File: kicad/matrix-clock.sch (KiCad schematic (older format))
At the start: 158 parts, among them P1 CONN_02X08, P2 CONN_01X03

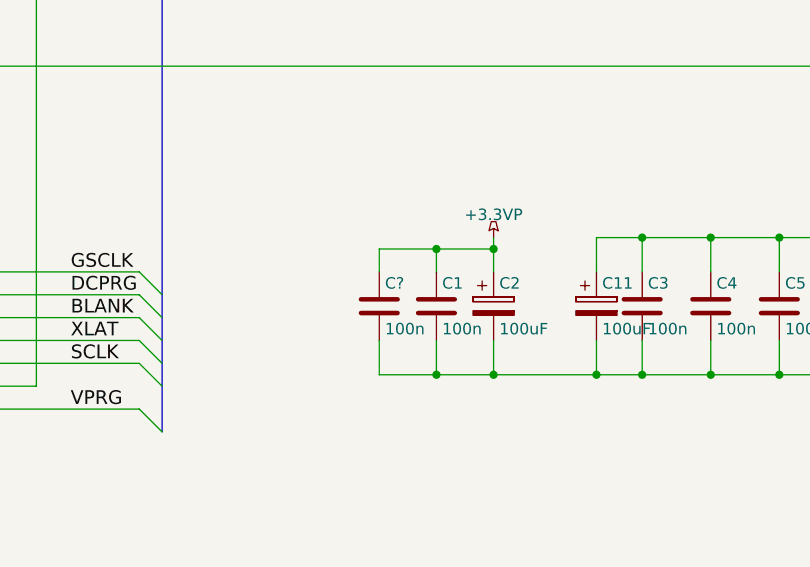
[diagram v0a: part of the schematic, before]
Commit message: removed libs
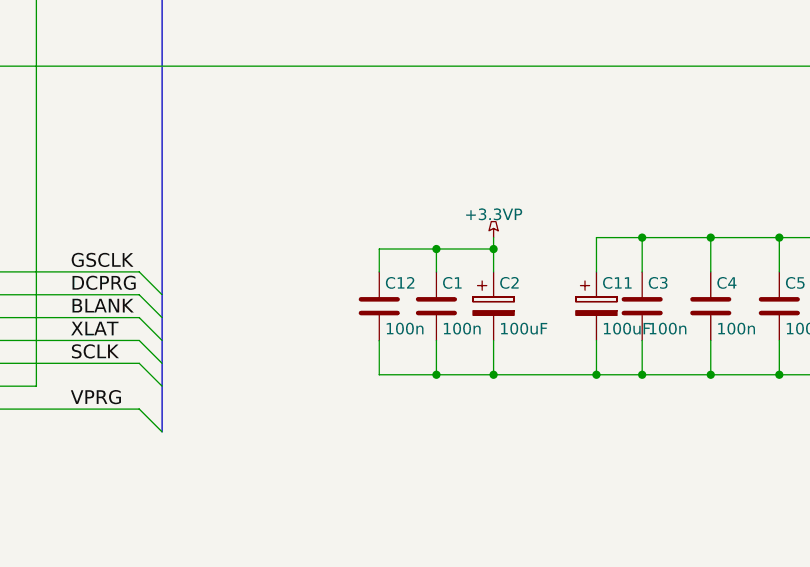
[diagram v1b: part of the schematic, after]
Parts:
- gave numbers to parts that had none: 1
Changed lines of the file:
@@
 LIBS:contrib
 LIBS:valves
-LIBS:IHE
-LIBS:open-project
 LIBS:matrix-clock-cache
 EELAYER 25 0
@@
 $EndComp
 $Comp
-L GND #PWR01
+L GND #PWR3
 U 1 1 57FAE61F
 P 1250 3050
-F 0 "#PWR01" H 1250 2800 50  0001 C CNN
+F 0 "#PWR3" H 1250 2800 50  0001 C CNN
 F 1 "GND" H 1250 2900 50  0000 C CNN
 F 2 "" H 1250 3050 50  0000 C CNN
@@
 $EndComp
 $Comp
-L +3.3VP #PWR02
+L +3.3VP #PWR1
 U 1 1 57FAE666
 P 650 650
-F 0 "#PWR02" H 800 600 50  0001 C CNN
+F 0 "#PWR1" H 800 600 50  0001 C CNN
 F 1 "+3.3VP" H 650 750 50  0000 C CNN
 F 2 "" H 650 650 50  0000 C CNN
@@
 $EndComp
 $Comp
-L +3.3V #PWR03
+L +3.3V #PWR5
 U 1 1 57FAE778
 P 1350 3250
-F 0 "#PWR03" H 1350 3100 50  0001 C CNN
+F 0 "#PWR5" H 1350 3100 50  0001 C CNN
 F 1 "+3.3V" H 1350 3390 50  0000 C CNN
 F 2 "" H 1350 3250 50  0000 C CNN
@@
 $EndComp
 $Comp
-L GND #PWR04
+L GND #PWR7
 U 1 1 57FAEBAA
 P 1550 3350
-F 0 "#PWR04" H 1550 3100 50  0001 C CNN
+F 0 "#PWR7" H 1550 3100 50  0001 C CNN
 F 1 "GND" H 1550 3200 50  0000 C CNN
 F 2 "" H 1550 3350 50  0000 C CNN
@@
 $EndComp
 $Comp
-L GND #PWR05
+L GND #PWR10
 U 1 1 57FB4A6F
 P 3000 3050
-F 0 "#PWR05" H 3000 2800 50  0001 C CNN
+F 0 "#PWR10" H 3000 2800 50  0001 C CNN
 F 1 "GND" H 3000 2900 50  0000 C CNN
 F 2 "" H 3000 3050 50  0000 C CNN
@@
 $EndComp
 $Comp
-L +3.3V #PWR06
+L +3.3V #PWR12
 U 1 1 57FB4A7B
 P 3100 3250
-F 0 "#PWR06" H 3100 3100 50  0001 C CNN
+F 0 "#PWR12" H 3100 3100 50  0001 C CNN
 F 1 "+3.3V" H 3100 3390 50  0000 C CNN
 F 2 "" H 3100 3250 50  0000 C CNN
@@
 $EndComp
 $Comp
-L GND #PWR07
+L GND #PWR14
 U 1 1 57FB4A89
 P 3300 3350
-F 0 "#PWR07" H 3300 3100 50  0001 C CNN
+F 0 "#PWR14" H 3300 3100 50  0001 C CNN
 F 1 "GND" H 3300 3200 50  0000 C CNN
 F 2 "" H 3300 3350 50  0000 C CNN
@@
 $EndComp
 $Comp
-L GND #PWR08
+L GND #PWR17
 U 1 1 57FB6FB4
 P 4750 3050
-F 0 "#PWR08" H 4750 2800 50  0001 C CNN
+F 0 "#PWR17" H 4750 2800 50  0001 C CNN
 F 1 "GND" H 4750 2900 50  0000 C CNN
 F 2 "" H 4750 3050 50  0000 C CNN
@@
 $EndComp
 $Comp
-L +3.3V #PWR09
+L +3.3V #PWR19
 U 1 1 57FB6FC0
 P 4850 3250
-F 0 "#PWR09" H 4850 3100 50  0001 C CNN
+F 0 "#PWR19" H 4850 3100 50  0001 C CNN
 F 1 "+3.3V" H 4850 3390 50  0000 C CNN
 F 2 "" H 4850 3250 50  0000 C CNN
@@
 $EndComp
 $Comp
-L GND #PWR010
+L GND #PWR20
 U 1 1 57FB6FCE
 P 5050 3350
-F 0 "#PWR010" H 5050 3100 50  0001 C CNN
+F 0 "#PWR20" H 5050 3100 50  0001 C CNN
 F 1 "GND" H 5050 3200 50  0000 C CNN
 F 2 "" H 5050 3350 50  0000 C CNN
@@
 $EndComp
 $Comp
-L GND #PWR011
+L GND #PWR22
 U 1 1 57FB707E
 P 6500 3050
-F 0 "#PWR011" H 6500 2800 50  0001 C CNN
+F 0 "#PWR22" H 6500 2800 50  0001 C CNN
 F 1 "GND" H 6500 2900 50  0000 C CNN
 F 2 "" H 6500 3050 50  0000 C CNN
@@
 $EndComp
 $Comp
-L +3.3V #PWR012
+L +3.3V #PWR23
 U 1 1 57FB7084
 P 6600 3250
-F 0 "#PWR012" H 6600 3100 50  0001 C CNN
+F 0 "#PWR23" H 6600 3100 50  0001 C CNN
 F 1 "+3.3V" H 6600 3390 50  0000 C CNN
 F 2 "" H 6600 3250 50  0000 C CNN
@@
 $EndComp
 $Comp
-L GND #PWR013
+L GND #PWR24
 U 1 1 57FB7092
 P 6800 3350
-F 0 "#PWR013" H 6800 3100 50  0001 C CNN
+F 0 "#PWR24" H 6800 3100 50  0001 C CNN
 F 1 "GND" H 6800 3200 50  0000 C CNN
 F 2 "" H 6800 3350 50  0000 C CNN
@@
 VPRG
 $Comp
-L GND #PWR014
+L GND #PWR35
 U 1 1 57FBA91D
 P 10600 6000
-F 0 "#PWR014" H 10600 5750 50  0001 C CNN
+F 0 "#PWR35" H 10600 5750 50  0001 C CNN
 F 1 "GND" H 10600 5850 50  0000 C CNN
 F 2 "" H 10600 6000 50  0000 C CNN
@@
 $EndComp
 $Comp
-L +3.3V #PWR015
+L +3.3V #PWR34
 U 1 1 57FBAA15
 P 10600 5400
-F 0 "#PWR015" H 10600 5250 50  0001 C CNN
+F 0 "#PWR34" H 10600 5250 50  0001 C CNN
 F 1 "+3.3V" H 10600 5540 50  0000 C CNN
 F 2 "" H 10600 5400 50  0000 C CNN
@@
 $EndComp
 $Comp
-L GND #PWR016
+L GND #PWR27
 U 1 1 57FC3799
 P 8250 3050
-F 0 "#PWR016" H 8250 2800 50  0001 C CNN
+F 0 "#PWR27" H 8250 2800 50  0001 C CNN
 F 1 "GND" H 8250 2900 50  0000 C CNN
 F 2 "" H 8250 3050 50  0000 C CNN
@@
 $EndComp
 $Comp
-L +3.3V #PWR017
+L +3.3V #PWR28
 U 1 1 57FC379F
 P 8350 3250
-F 0 "#PWR017" H 8350 3100 50  0001 C CNN
+F 0 "#PWR28" H 8350 3100 50  0001 C CNN
 F 1 "+3.3V" H 8350 3390 50  0000 C CNN
 F 2 "" H 8350 3250 50  0000 C CNN
@@
 $EndComp
 $Comp
-L GND #PWR018
+L GND #PWR29
 U 1 1 57FC37AB
 P 8550 3350
-F 0 "#PWR018" H 8550 3100 50  0001 C CNN
+F 0 "#PWR29" H 8550 3100 50  0001 C CNN
 F 1 "GND" H 8550 3200 50  0000 C CNN
 F 2 "" H 8550 3350 50  0000 C CNN
@@
 $EndComp
 $Comp
-L GND #PWR019
+L GND #PWR31
 U 1 1 57FC44F1
 P 10000 3050
-F 0 "#PWR019" H 10000 2800 50  0001 C CNN
+F 0 "#PWR31" H 10000 2800 50  0001 C CNN
 F 1 "GND" H 10000 2900 50  0000 C CNN
 F 2 "" H 10000 3050 50  0000 C CNN
@@
 $EndComp
 $Comp
-L +3.3V #PWR020
+L +3.3V #PWR32
 U 1 1 57FC44F7
 P 10100 3250
-F 0 "#PWR020" H 10100 3100 50  0001 C CNN
+F 0 "#PWR32" H 10100 3100 50  0001 C CNN
 F 1 "+3.3V" H 10100 3390 50  0000 C CNN
 F 2 "" H 10100 3250 50  0000 C CNN
@@
 $EndComp
 $Comp
-L GND #PWR021
+L GND #PWR33
 U 1 1 57FC4503
 P 10300 3350
-F 0 "#PWR021" H 10300 3100 50  0001 C CNN
+F 0 "#PWR33" H 10300 3100 50  0001 C CNN
 F 1 "GND" H 10300 3200 50  0000 C CNN
 F 2 "" H 10300 3350 50  0000 C CNN
@@
 DCPRG
 $Comp
-L +3.3VP #PWR022
+L +3.3VP #PWR25
 U 1 1 57FD372C
 P 7600 5400
-F 0 "#PWR022" H 7750 5350 50  0001 C CNN
+F 0 "#PWR25" H 7750 5350 50  0001 C CNN
 F 1 "+3.3VP" H 7600 5500 50  0000 C CNN
 F 2 "" H 7600 5400 50  0000 C CNN
@@
 $EndComp
 $Comp
-L GND #PWR023
+L GND #PWR4
 U 1 1 57FDA5D3
 P 1250 5150
-F 0 "#PWR023" H 1250 4900 50  0001 C CNN
+F 0 "#PWR4" H 1250 4900 50  0001 C CNN
 F 1 "GND" H 1250 5000 50  0000 C CNN
 F 2 "" H 1250 5150 50  0000 C CNN
@@
 $EndComp
 $Comp
-L +3.3V #PWR024
+L +3.3V #PWR6
 U 1 1 57FDA5DF
 P 1350 4950
-F 0 "#PWR024" H 1350 4800 50  0001 C CNN
+F 0 "#PWR6" H 1350 4800 50  0001 C CNN
 F 1 "+3.3V" H 1350 5090 50  0000 C CNN
 F 2 "" H 1350 4950 50  0000 C CNN
@@
 $EndComp
 $Comp
-L GND #PWR025
+L GND #PWR8
 U 1 1 57FDA5EB
 P 1550 4900
-F 0 "#PWR025" H 1550 4650 50  0001 C CNN
+F 0 "#PWR8" H 1550 4650 50  0001 C CNN
 F 1 "GND" H 1550 4750 50  0000 C CNN
 F 2 "" H 1550 4900 50  0000 C CNN
@@
 $EndComp
 $Comp
-L GND #PWR026
+L GND #PWR11
 U 1 1 57FDA663
 P 3000 5150
-F 0 "#PWR026" H 3000 4900 50  0001 C CNN
+F 0 "#PWR11" H 3000 4900 50  0001 C CNN
 F 1 "GND" H 3000 5000 50  0000 C CNN
 F 2 "" H 3000 5150 50  0000 C CNN
@@
 $EndComp
 $Comp
-L +3.3V #PWR027
+L +3.3V #PWR13
 U 1 1 57FDA669
 P 3100 4950
-F 0 "#PWR027" H 3100 4800 50  0001 C CNN
+F 0 "#PWR13" H 3100 4800 50  0001 C CNN
 F 1 "+3.3V" H 3100 5090 50  0000 C CNN
 F 2 "" H 3100 4950 50  0000 C CNN
@@
 $EndComp
 $Comp
-L GND #PWR028
+L GND #PWR15
 U 1 1 57FDA675
 P 3300 4900
-F 0 "#PWR028" H 3300 4650 50  0001 C CNN
+F 0 "#PWR15" H 3300 4650 50  0001 C CNN
 F 1 "GND" H 3300 4750 50  0000 C CNN
 F 2 "" H 3300 4900 50  0000 C CNN
@@
 $EndComp
 $Comp
-L +3.3VP #PWR029
+L +3.3VP #PWR2
 U 1 1 57FF26B5
 P 650 7400
-F 0 "#PWR029" H 800 7350 50  0001 C CNN
+F 0 "#PWR2" H 800 7350 50  0001 C CNN
 F 1 "+3.3VP" H 650 7500 50  0000 C CNN
 F 2 "" H 650 7400 50  0000 C CNN
@@
 $EndComp
 $Comp
-L +3.3VP #PWR030
+L +3.3VP #PWR9
 U 1 1 57FF3E3B
 P 2400 650
-F 0 "#PWR030" H 2550 600 50  0001 C CNN
+F 0 "#PWR9" H 2550 600 50  0001 C CNN
 F 1 "+3.3VP" H 2400 750 50  0000 C CNN
 F 2 "" H 2400 650 50  0000 C CNN
@@
 $EndComp
 $Comp
-L +3.3VP #PWR031
+L +3.3VP #PWR16
 U 1 1 57FF4355
 P 4150 650
-F 0 "#PWR031" H 4300 600 50  0001 C CNN
+F 0 "#PWR16" H 4300 600 50  0001 C CNN
 F 1 "+3.3VP" H 4150 750 50  0000 C CNN
 F 2 "" H 4150 650 50  0000 C CNN
@@
 $EndComp
 $Comp
-L +3.3VP #PWR032
+L +3.3VP #PWR21
 U 1 1 57FF4834
 P 5900 650
-F 0 "#PWR032" H 6050 600 50  0001 C CNN
+F 0 "#PWR21" H 6050 600 50  0001 C CNN
 F 1 "+3.3VP" H 5900 750 50  0000 C CNN
 F 2 "" H 5900 650 50  0000 C CNN
@@
 $EndComp
 $Comp
-L +3.3VP #PWR033
+L +3.3VP #PWR26
 U 1 1 57FF557A
 P 7650 650
-F 0 "#PWR033" H 7800 600 50  0001 C CNN
+F 0 "#PWR26" H 7800 600 50  0001 C CNN
 F 1 "+3.3VP" H 7650 750 50  0000 C CNN
 F 2 "" H 7650 650 50  0000 C CNN
@@
 $EndComp
 $Comp
-L +3.3VP #PWR034
+L +3.3VP #PWR30
 U 1 1 57FF5BD9
 P 9400 650
-F 0 "#PWR034" H 9550 600 50  0001 C CNN
+F 0 "#PWR30" H 9550 600 50  0001 C CNN
 F 1 "+3.3VP" H 9400 750 50  0000 C CNN
 F 2 "" H 9400 650 50  0000 C CNN
@@
 $EndComp
 $Comp
-L GND #PWR035
+L GND #PWR18
 U 1 1 5800335E
 P 4800 6350
-F 0 "#PWR035" H 4800 6100 50  0001 C CNN
+F 0 "#PWR18" H 4800 6100 50  0001 C CNN
 F 1 "GND" H 4800 6200 50  0000 C CNN
 F 2 "" H 4800 6350 50  0000 C CNN
@@
 $EndComp
 $Comp
-L +3.3VP #PWR036
+L +3.3VP #PWR36
 U 1 1 58017B29
 P 10650 5800
-F 0 "#PWR036" H 10800 5750 50  0001 C CNN
+F 0 "#PWR36" H 10800 5750 50  0001 C CNN
 F 1 "+3.3VP" H 10650 5900 50  0000 C CNN
 F 2 "" H 10650 5800 50  0000 C CNN
@@
 $EndComp
 $Comp
-L C C?
+L C C12
 U 1 1 5801A712
 P 7100 5700
-F 0 "C?" H 7125 5800 50  0000 L CNN
+F 0 "C12" H 7125 5800 50  0000 L CNN
 F 1 "100n" H 7125 5600 50  0000 L CNN
 F 2 "Capacitors_SMD:C_0603_HandSoldering" H 7138 5550 50  0001 C CNN

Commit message: pcb fixes
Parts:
- removed C12: 100n, Capacitors_SMD:C_0603_HandSoldering, symbol C
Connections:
- net BLANK: now also P1.10 (P10); no longer P1.8 (P8)
- net DCPRG: now also P1.12 (P12); no longer P1.6 (P6)
- net GND: no longer C1.2, C10.2, C11.2, C2.2, C3.2, C4.2, C5.2, C6.2, C7.2, C8.2, C9.2
- net GSCLK: now also P1.14 (P14); no longer P1.4 (P4)
- net SCLK: now also P1.6 (P6); no longer P1.12 (P12)
- net VPRG: now also P1.2 (P2); no longer P1.16 (P16)
- net XLAT: now also P1.8 (P8); no longer P1.10 (P10)
- net at TLC1.26 (SIN): now also P1.4 (P4); no longer P1.14 (P14)
- new net: C1.2, C2.2
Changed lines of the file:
@@
 $EndComp
 $Comp
-L GND #PWR3
+L GND #PWR01
 U 1 1 57FAE61F
 P 1250 3050
-F 0 "#PWR3" H 1250 2800 50  0001 C CNN
+F 0 "#PWR01" H 1250 2800 50  0001 C CNN
 F 1 "GND" H 1250 2900 50  0000 C CNN
 F 2 "" H 1250 3050 50  0000 C CNN
@@
 $EndComp
 $Comp
-L +3.3VP #PWR1
+L +3.3VP #PWR02
 U 1 1 57FAE666
 P 650 650
-F 0 "#PWR1" H 800 600 50  0001 C CNN
+F 0 "#PWR02" H 800 600 50  0001 C CNN
 F 1 "+3.3VP" H 650 750 50  0000 C CNN
 F 2 "" H 650 650 50  0000 C CNN
@@
 $EndComp
 $Comp
-L +3.3V #PWR5
+L +3.3V #PWR03
 U 1 1 57FAE778
 P 1350 3250
-F 0 "#PWR5" H 1350 3100 50  0001 C CNN
+F 0 "#PWR03" H 1350 3100 50  0001 C CNN
 F 1 "+3.3V" H 1350 3390 50  0000 C CNN
 F 2 "" H 1350 3250 50  0000 C CNN
@@
 $EndComp
 $Comp
-L GND #PWR7
+L GND #PWR04
 U 1 1 57FAEBAA
 P 1550 3350
-F 0 "#PWR7" H 1550 3100 50  0001 C CNN
+F 0 "#PWR04" H 1550 3100 50  0001 C CNN
 F 1 "GND" H 1550 3200 50  0000 C CNN
 F 2 "" H 1550 3350 50  0000 C CNN
@@
 $EndComp
 $Comp
-L GND #PWR10
+L GND #PWR05
 U 1 1 57FB4A6F
 P 3000 3050
-F 0 "#PWR10" H 3000 2800 50  0001 C CNN
+F 0 "#PWR05" H 3000 2800 50  0001 C CNN
 F 1 "GND" H 3000 2900 50  0000 C CNN
 F 2 "" H 3000 3050 50  0000 C CNN
@@
 $EndComp
 $Comp
-L +3.3V #PWR12
+L +3.3V #PWR06
 U 1 1 57FB4A7B
 P 3100 3250
-F 0 "#PWR12" H 3100 3100 50  0001 C CNN
+F 0 "#PWR06" H 3100 3100 50  0001 C CNN
 F 1 "+3.3V" H 3100 3390 50  0000 C CNN
 F 2 "" H 3100 3250 50  0000 C CNN
@@
 $EndComp
 $Comp
-L GND #PWR14
+L GND #PWR07
 U 1 1 57FB4A89
 P 3300 3350
-F 0 "#PWR14" H 3300 3100 50  0001 C CNN
+F 0 "#PWR07" H 3300 3100 50  0001 C CNN
 F 1 "GND" H 3300 3200 50  0000 C CNN
 F 2 "" H 3300 3350 50  0000 C CNN
@@
 $EndComp
 $Comp
-L GND #PWR17
+L GND #PWR08
 U 1 1 57FB6FB4
 P 4750 3050
-F 0 "#PWR17" H 4750 2800 50  0001 C CNN
+F 0 "#PWR08" H 4750 2800 50  0001 C CNN
 F 1 "GND" H 4750 2900 50  0000 C CNN
 F 2 "" H 4750 3050 50  0000 C CNN
@@
 $EndComp
 $Comp
-L +3.3V #PWR19
+L +3.3V #PWR09
 U 1 1 57FB6FC0
 P 4850 3250
-F 0 "#PWR19" H 4850 3100 50  0001 C CNN
+F 0 "#PWR09" H 4850 3100 50  0001 C CNN
 F 1 "+3.3V" H 4850 3390 50  0000 C CNN
 F 2 "" H 4850 3250 50  0000 C CNN
@@
 $EndComp
 $Comp
-L GND #PWR20
+L GND #PWR010
 U 1 1 57FB6FCE
 P 5050 3350
-F 0 "#PWR20" H 5050 3100 50  0001 C CNN
+F 0 "#PWR010" H 5050 3100 50  0001 C CNN
 F 1 "GND" H 5050 3200 50  0000 C CNN
 F 2 "" H 5050 3350 50  0000 C CNN
@@
 $EndComp
 $Comp
-L GND #PWR22
+L GND #PWR011
 U 1 1 57FB707E
 P 6500 3050
-F 0 "#PWR22" H 6500 2800 50  0001 C CNN
+F 0 "#PWR011" H 6500 2800 50  0001 C CNN
 F 1 "GND" H 6500 2900 50  0000 C CNN
 F 2 "" H 6500 3050 50  0000 C CNN
@@
 $EndComp
 $Comp
-L +3.3V #PWR23
+L +3.3V #PWR012
 U 1 1 57FB7084
 P 6600 3250
-F 0 "#PWR23" H 6600 3100 50  0001 C CNN
+F 0 "#PWR012" H 6600 3100 50  0001 C CNN
 F 1 "+3.3V" H 6600 3390 50  0000 C CNN
 F 2 "" H 6600 3250 50  0000 C CNN
@@
 $EndComp
 $Comp
-L GND #PWR24
+L GND #PWR013
 U 1 1 57FB7092
 P 6800 3350
-F 0 "#PWR24" H 6800 3100 50  0001 C CNN
+F 0 "#PWR013" H 6800 3100 50  0001 C CNN
 F 1 "GND" H 6800 3200 50  0000 C CNN
 F 2 "" H 6800 3350 50  0000 C CNN
@@
 VPRG
 $Comp
-L GND #PWR35
+L GND #PWR014
 U 1 1 57FBA91D
 P 10600 6000
-F 0 "#PWR35" H 10600 5750 50  0001 C CNN
+F 0 "#PWR014" H 10600 5750 50  0001 C CNN
 F 1 "GND" H 10600 5850 50  0000 C CNN
 F 2 "" H 10600 6000 50  0000 C CNN
@@
 $EndComp
 $Comp
-L +3.3V #PWR34
+L +3.3V #PWR015
 U 1 1 57FBAA15
 P 10600 5400
-F 0 "#PWR34" H 10600 5250 50  0001 C CNN
+F 0 "#PWR015" H 10600 5250 50  0001 C CNN
 F 1 "+3.3V" H 10600 5540 50  0000 C CNN
 F 2 "" H 10600 5400 50  0000 C CNN
@@
 $EndComp
 $Comp
-L GND #PWR27
+L GND #PWR016
 U 1 1 57FC3799
 P 8250 3050
-F 0 "#PWR27" H 8250 2800 50  0001 C CNN
+F 0 "#PWR016" H 8250 2800 50  0001 C CNN
 F 1 "GND" H 8250 2900 50  0000 C CNN
 F 2 "" H 8250 3050 50  0000 C CNN
@@
 $EndComp
 $Comp
-L +3.3V #PWR28
+L +3.3V #PWR017
 U 1 1 57FC379F
 P 8350 3250
-F 0 "#PWR28" H 8350 3100 50  0001 C CNN
+F 0 "#PWR017" H 8350 3100 50  0001 C CNN
 F 1 "+3.3V" H 8350 3390 50  0000 C CNN
 F 2 "" H 8350 3250 50  0000 C CNN
@@
 $EndComp
 $Comp
-L GND #PWR29
+L GND #PWR018
 U 1 1 57FC37AB
 P 8550 3350
-F 0 "#PWR29" H 8550 3100 50  0001 C CNN
+F 0 "#PWR018" H 8550 3100 50  0001 C CNN
 F 1 "GND" H 8550 3200 50  0000 C CNN
 F 2 "" H 8550 3350 50  0000 C CNN
@@
 $EndComp
 $Comp
-L GND #PWR31
+L GND #PWR019
 U 1 1 57FC44F1
 P 10000 3050
-F 0 "#PWR31" H 10000 2800 50  0001 C CNN
+F 0 "#PWR019" H 10000 2800 50  0001 C CNN
 F 1 "GND" H 10000 2900 50  0000 C CNN
 F 2 "" H 10000 3050 50  0000 C CNN
@@
 $EndComp
 $Comp
-L +3.3V #PWR32
+L +3.3V #PWR020
 U 1 1 57FC44F7
 P 10100 3250
-F 0 "#PWR32" H 10100 3100 50  0001 C CNN
+F 0 "#PWR020" H 10100 3100 50  0001 C CNN
 F 1 "+3.3V" H 10100 3390 50  0000 C CNN
 F 2 "" H 10100 3250 50  0000 C CNN
@@
 $EndComp
 $Comp
-L GND #PWR33
+L GND #PWR021
 U 1 1 57FC4503
 P 10300 3350
-F 0 "#PWR33" H 10300 3100 50  0001 C CNN
+F 0 "#PWR021" H 10300 3100 50  0001 C CNN
 F 1 "GND" H 10300 3200 50  0000 C CNN
 F 2 "" H 10300 3350 50  0000 C CNN
@@
 F 3 "" H 5100 4600 50  0000 C CNN
 	1    5100 5800
-	1    0    0    -1
+	1    0    0    1
 $EndComp
 Entry Wire Line
@@
 DCPRG
 $Comp
-L +3.3VP #PWR25
+L +3.3VP #PWR022
 U 1 1 57FD372C
 P 7600 5400
-F 0 "#PWR25" H 7750 5350 50  0001 C CNN
+F 0 "#PWR022" H 7750 5350 50  0001 C CNN
 F 1 "+3.3VP" H 7600 5500 50  0000 C CNN
 F 2 "" H 7600 5400 50  0000 C CNN
@@
 $EndComp
 $Comp
-L GND #PWR4
+L GND #PWR023
 U 1 1 57FDA5D3
 P 1250 5150
-F 0 "#PWR4" H 1250 4900 50  0001 C CNN
+F 0 "#PWR023" H 1250 4900 50  0001 C CNN
 F 1 "GND" H 1250 5000 50  0000 C CNN
 F 2 "" H 1250 5150 50  0000 C CNN
@@
 $EndComp
 $Comp
-L +3.3V #PWR6
+L +3.3V #PWR024
 U 1 1 57FDA5DF
 P 1350 4950
-F 0 "#PWR6" H 1350 4800 50  0001 C CNN
+F 0 "#PWR024" H 1350 4800 50  0001 C CNN
 F 1 "+3.3V" H 1350 5090 50  0000 C CNN
 F 2 "" H 1350 4950 50  0000 C CNN
@@
 $EndComp
 $Comp
-L GND #PWR8
+L GND #PWR025
 U 1 1 57FDA5EB
 P 1550 4900
-F 0 "#PWR8" H 1550 4650 50  0001 C CNN
+F 0 "#PWR025" H 1550 4650 50  0001 C CNN
 F 1 "GND" H 1550 4750 50  0000 C CNN
 F 2 "" H 1550 4900 50  0000 C CNN
@@
 $EndComp
 $Comp
-L GND #PWR11
+L GND #PWR026
 U 1 1 57FDA663
 P 3000 5150
-F 0 "#PWR11" H 3000 4900 50  0001 C CNN
+F 0 "#PWR026" H 3000 4900 50  0001 C CNN
 F 1 "GND" H 3000 5000 50  0000 C CNN
 F 2 "" H 3000 5150 50  0000 C CNN
@@
 $EndComp
 $Comp
-L +3.3V #PWR13
+L +3.3V #PWR027
 U 1 1 57FDA669
 P 3100 4950
-F 0 "#PWR13" H 3100 4800 50  0001 C CNN
+F 0 "#PWR027" H 3100 4800 50  0001 C CNN
 F 1 "+3.3V" H 3100 5090 50  0000 C CNN
 F 2 "" H 3100 4950 50  0000 C CNN
@@
 $EndComp
 $Comp
-L GND #PWR15
+L GND #PWR028
 U 1 1 57FDA675
 P 3300 4900
-F 0 "#PWR15" H 3300 4650 50  0001 C CNN
+F 0 "#PWR028" H 3300 4650 50  0001 C CNN
 F 1 "GND" H 3300 4750 50  0000 C CNN
 F 2 "" H 3300 4900 50  0000 C CNN
@@
 $EndComp
 $Comp
-L +3.3VP #PWR2
+L +3.3VP #PWR029
 U 1 1 57FF26B5
 P 650 7400
-F 0 "#PWR2" H 800 7350 50  0001 C CNN
+F 0 "#PWR029" H 800 7350 50  0001 C CNN
 F 1 "+3.3VP" H 650 7500 50  0000 C CNN
 F 2 "" H 650 7400 50  0000 C CNN
@@
 $EndComp
 $Comp
-L +3.3VP #PWR9
+L +3.3VP #PWR030
 U 1 1 57FF3E3B
 P 2400 650
-F 0 "#PWR9" H 2550 600 50  0001 C CNN
+F 0 "#PWR030" H 2550 600 50  0001 C CNN
 F 1 "+3.3VP" H 2400 750 50  0000 C CNN
 F 2 "" H 2400 650 50  0000 C CNN
@@
 $EndComp
 $Comp
-L +3.3VP #PWR16
+L +3.3VP #PWR031
 U 1 1 57FF4355
 P 4150 650
-F 0 "#PWR16" H 4300 600 50  0001 C CNN
+F 0 "#PWR031" H 4300 600 50  0001 C CNN
 F 1 "+3.3VP" H 4150 750 50  0000 C CNN
 F 2 "" H 4150 650 50  0000 C CNN
@@
 $EndComp
 $Comp
-L +3.3VP #PWR21
+L +3.3VP #PWR032
 U 1 1 57FF4834
 P 5900 650
-F 0 "#PWR21" H 6050 600 50  0001 C CNN
+F 0 "#PWR032" H 6050 600 50  0001 C CNN
 F 1 "+3.3VP" H 5900 750 50  0000 C CNN
 F 2 "" H 5900 650 50  0000 C CNN
@@
 $EndComp
 $Comp
-L +3.3VP #PWR26
+L +3.3VP #PWR033
 U 1 1 57FF557A
 P 7650 650
-F 0 "#PWR26" H 7800 600 50  0001 C CNN
+F 0 "#PWR033" H 7800 600 50  0001 C CNN
 F 1 "+3.3VP" H 7650 750 50  0000 C CNN
 F 2 "" H 7650 650 50  0000 C CNN
@@
 $EndComp
 $Comp
-L +3.3VP #PWR30
+L +3.3VP #PWR034
 U 1 1 57FF5BD9
 P 9400 650
-F 0 "#PWR30" H 9550 600 50  0001 C CNN
+F 0 "#PWR034" H 9550 600 50  0001 C CNN
 F 1 "+3.3VP" H 9400 750 50  0000 C CNN
 F 2 "" H 9400 650 50  0000 C CNN
@@
 $EndComp
 $Comp
-L GND #PWR18
+L GND #PWR035
 U 1 1 5800335E
 P 4800 6350
-F 0 "#PWR18" H 4800 6100 50  0001 C CNN
+F 0 "#PWR035" H 4800 6100 50  0001 C CNN
 F 1 "GND" H 4800 6200 50  0000 C CNN
 F 2 "" H 4800 6350 50  0000 C CNN
@@
 $EndComp
 $Comp
-L +3.3VP #PWR36
+L +3.3VP #PWR036
 U 1 1 58017B29
 P 10650 5800
-F 0 "#PWR36" H 10800 5750 50  0001 C CNN
+F 0 "#PWR036" H 10800 5750 50  0001 C CNN
 F 1 "+3.3VP" H 10650 5900 50  0000 C CNN
 F 2 "" H 10650 5800 50  0000 C CNN
@@
 	1    0    0    -1
 $EndComp
-$Comp
-L C C12
-U 1 1 5801A712
-P 7100 5700
-F 0 "C12" H 7125 5800 50  0000 L CNN
-F 1 "100n" H 7125 5600 50  0000 L CNN
-F 2 "Capacitors_SMD:C_0603_HandSoldering" H 7138 5550 50  0001 C CNN
-F 3 "" H 7100 5700 50  0000 C CNN
-	1    7100 5700
-	1    0    0    -1
-$EndComp
 Connection ~ 650  650
 Connection ~ 2050 650
@@
 	10650 5600 10600 5600
 Wire Wire Line
-	10600 5600 10600 5400
+	10600 5400 10600 5600
 Connection ~ 4800 6150
 Wire Wire Line
-	10600 5400 8050 5400
-Wire Wire Line
-	7100 6000 10600 6000
+	8050 5400 10600 5400
 Wire Wire Line
 	5350 5750 6050 5750
@@
 	8050 5850 8050 6000
 Connection ~ 8050 6000
-Wire Wire Line
-	7350 5850 7350 6000
 Connection ~ 7600 6000
+Connection ~ 7600 5450
 Wire Wire Line
-	7350 5550 7350 5450
+	7350 5850 7350 6000
 Wire Wire Line
-	7100 5450 7600 5450
-Connection ~ 7600 5450
+	7350 6000 7600 6000
 Wire Wire Line
-	7100 5450 7100 5550
-Connection ~ 7350 5450
+	7350 5550 7350 5450
 Wire Wire Line
-	7100 6000 7100 5850
-Connection ~ 7350 6000
+	7350 5450 7600 5450
 $EndSCHEMATC
